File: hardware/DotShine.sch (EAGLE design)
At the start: 55 parts, among them CN1 1X4-BIG, IC1 CAT24M010TS, IC3 SI1145, J3 USB-MICROB, U1 ATMEGA328P-MU-QFN32, U2 TMP102, U3 ATSHA204-TSU, X2 MC-RTC-RV-4162-C7-I2C, X3 S4B-ZR

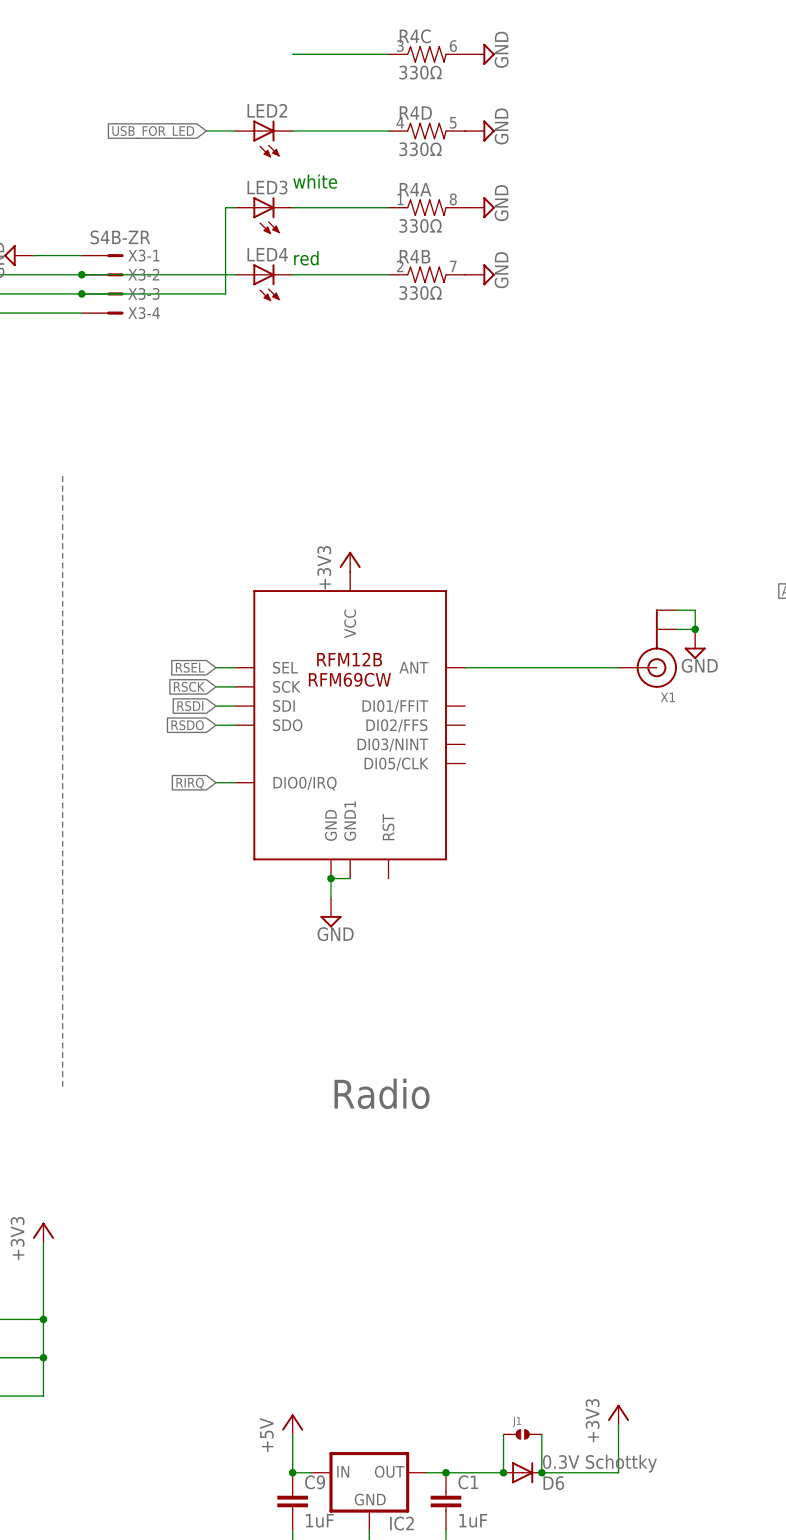
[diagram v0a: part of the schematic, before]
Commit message: Add RST led
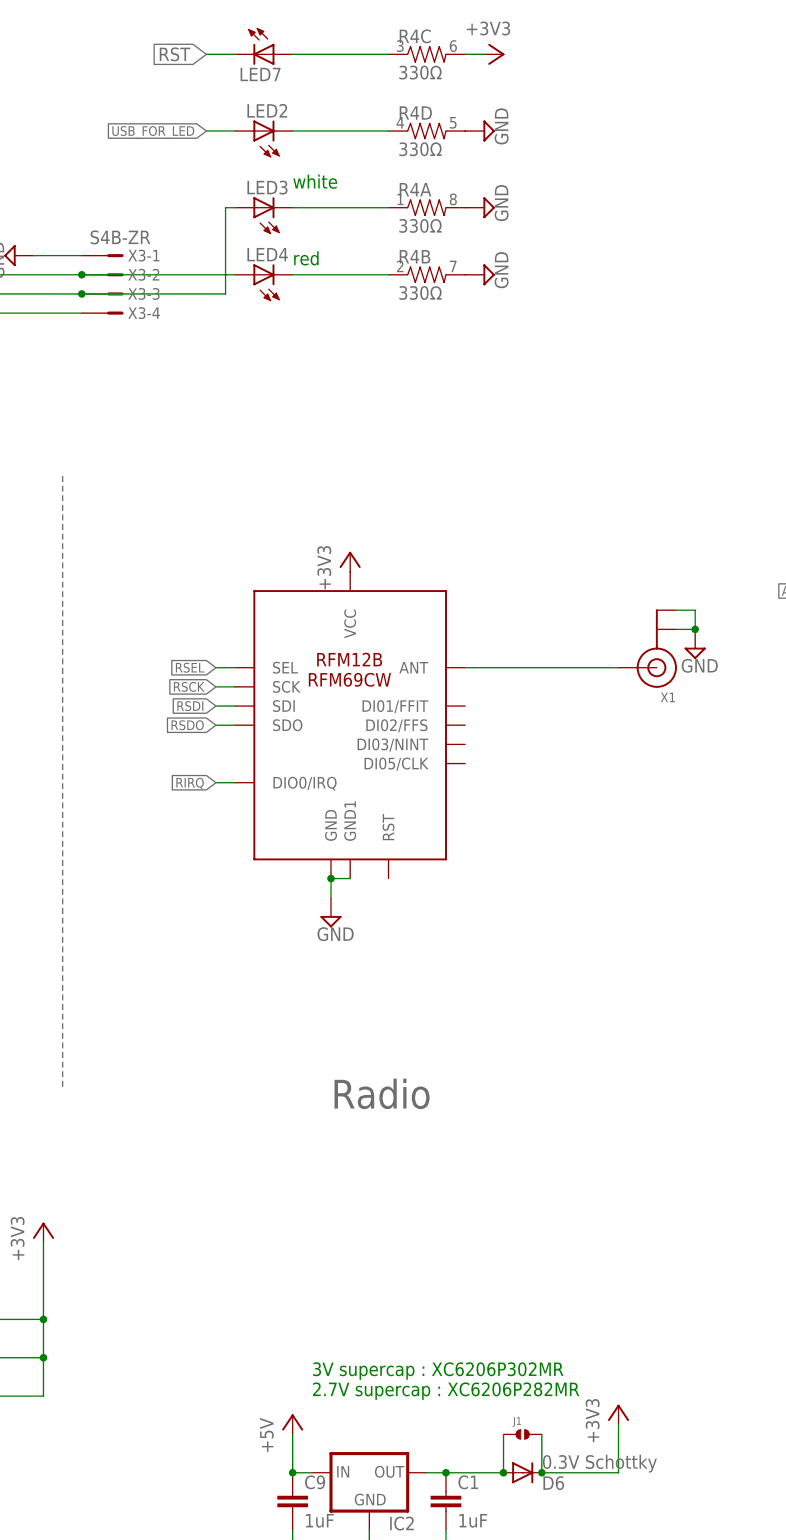
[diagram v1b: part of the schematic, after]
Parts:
- added LED7: (no value), SparkFun:LED0603
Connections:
- net +3V3: now also R4C.2
- net GND: no longer R4C.2
- net N$10: now also LED7.A
- net RST: now also LED7.C
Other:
- note added: "3V supercap : XC6206P302MR 2.7V supercap : XC6206P282MR"
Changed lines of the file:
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@@
 <setting verticaltext="up"/>
 </settings>
-<grid distance="0.1" unitdist="inch" unit="inch" style="lines" multiple="1" display="no" altdistance="0.01" altunitdist="inch" altunit="inch"/>
+<grid distance="0.05" unitdist="inch" unit="inch" style="lines" multiple="1" display="no" altdistance="0.01" altunitdist="inch" altunit="inch"/>
 <layers>
 <layer number="1" name="Top" color="4" fill="1" visible="no" active="no"/>
@@
 <part name="+3V7" library="supply1" deviceset="+3V3" device=""/>
 <part name="R4" library="SparkFun" deviceset="RESISTOR-ARRAY" device="0603-ARV" value="330Ω"/>
-<part name="SUPPLY12" library="supply2" deviceset="GND" device=""/>
 <part name="SUPPLY27" library="supply2" deviceset="GND" device=""/>
 <part name="+3V19" library="supply1" deviceset="+3V3" device=""/>
@@
 <part name="P+5" library="supply1" deviceset="+5V" device=""/>
 <part name="D4" library="diode" deviceset="DIODE-" device="SOD523" value="0.3V Schottky"/>
+<part name="+3V1" library="supply1" deviceset="+3V3" device=""/>
+<part name="LED7" library="SparkFun" deviceset="LED" device="0603"/>
 </parts>
 <sheets>
@@
 <text x="30.48" y="-243.84" size="1.778" layer="91">1000uF .. 6V -&gt; 300uF .. 2V ; 600 .. 3.6V -&gt; buget: 600-300 = 300uF
 1500uF .. 4V -&gt; 750uF .. 2V ; 1350.. 3.6V-&gt; buget: 1350-750 = 600uF</text>
+<text x="137.16" y="-25.4" size="1.778" layer="91">3V supercap : XC6206P302MR
+2.7V supercap : XC6206P282MR</text>
 </plain>
 <instances>
@@
 <instance part="R4" gate="C" x="152.4" y="152.4"/>
 <instance part="R4" gate="D" x="152.4" y="142.24"/>
-<instance part="SUPPLY12" gate="GND" x="160.02" y="152.4" rot="R90"/>
 <instance part="SUPPLY27" gate="GND" x="144.78" y="-48.26" rot="MR0"/>
 <instance part="+3V19" gate="G$1" x="177.8" y="-26.67"/>
@@
 <instance part="P+5" gate="1" x="31.75" y="-205.74"/>
 <instance part="D4" gate="G$1" x="69.85" y="-48.26" rot="MR0"/>
+<instance part="+3V1" gate="G$1" x="162.56" y="152.4" rot="R270"/>
+<instance part="LED7" gate="G$1" x="132.08" y="152.4" rot="R270"/>
 </instances>
 <busses>
@@
 <pinref part="SUPPLY8" gate="GND" pin="GND"/>
 <pinref part="R4" gate="A" pin="2"/>
-</segment>
-<segment>
-<pinref part="R4" gate="C" pin="2"/>
-<pinref part="SUPPLY12" gate="GND" pin="GND"/>
 </segment>
 <segment>
@@
 <wire x1="60.96" y1="118.11" x2="52.07" y2="118.11" width="0.1524" layer="91"/>
 <label x="52.07" y="118.11" size="1.27" layer="95" rot="R180" xref="yes"/>
+</segment>
+<segment>
+<pinref part="LED7" gate="G$1" pin="C"/>
+<wire x1="127" y1="152.4" x2="123.19" y2="152.4" width="0.1524" layer="91"/>
+<label x="123.19" y="152.4" size="1.778" layer="95" rot="R180" xref="yes"/>
 </segment>
 </net>
@@
 <wire x1="167.64" y1="-35.56" x2="177.8" y2="-35.56" width="0.1524" layer="91"/>
 <wire x1="177.8" y1="-35.56" x2="177.8" y2="-29.21" width="0.1524" layer="91"/>
+</segment>
+<segment>
+<pinref part="R4" gate="C" pin="2"/>
+<pinref part="+3V1" gate="G$1" pin="+3V3"/>
+<wire x1="157.48" y1="152.4" x2="160.02" y2="152.4" width="0.1524" layer="91"/>
 </segment>
 </net>
@@
 </segment>
 </net>
-<net name="N$10" class="0">
-<segment>
-<pinref part="R4" gate="C" pin="1"/>
-<wire x1="147.32" y1="152.4" x2="134.62" y2="152.4" width="0.1524" layer="91"/>
-</segment>
-</net>
 <net name="N$11" class="0">
 <segment>
@@
 </segment>
 </net>
+<net name="N$10" class="0">
+<segment>
+<pinref part="LED7" gate="G$1" pin="A"/>
+<pinref part="R4" gate="C" pin="1"/>
+<wire x1="134.62" y1="152.4" x2="147.32" y2="152.4" width="0.1524" layer="91"/>
+</segment>
+</net>

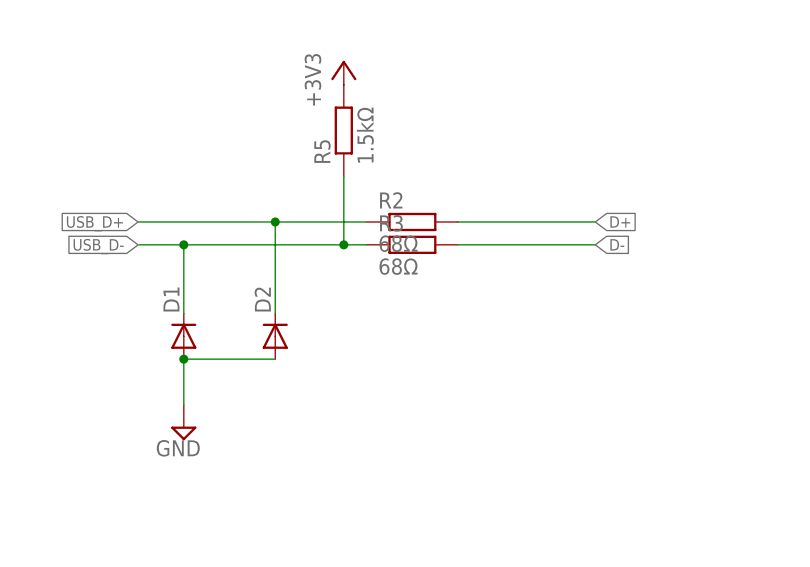
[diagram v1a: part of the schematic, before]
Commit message: Invert cap, improve GND
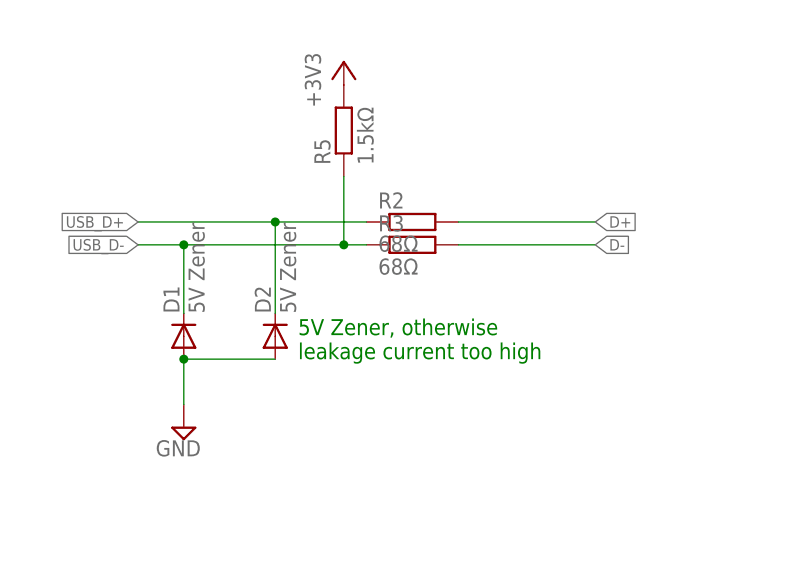
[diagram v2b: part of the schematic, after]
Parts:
- D1, D2: value (none) -> 5V Zener
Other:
- note added: "5V Zener, otherwise leakage current too high"
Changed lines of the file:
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@@
 <setting verticaltext="up"/>
 </settings>
-<grid distance="0.05" unitdist="inch" unit="inch" style="lines" multiple="1" display="no" altdistance="0.01" altunitdist="inch" altunit="inch"/>
+<grid distance="0.1" unitdist="inch" unit="inch" style="lines" multiple="1" display="no" altdistance="0.01" altunitdist="inch" altunit="inch"/>
 <layers>
 <layer number="1" name="Top" color="4" fill="1" visible="no" active="no"/>
@@
 <part name="+3V12" library="supply1" deviceset="+3V3" device=""/>
 <part name="JP2" library="SparkFun-Jumpers" deviceset="JUMPER-SMT_3_1-NC_TRACE" device="_NO-SILK"/>
-<part name="D1" library="diode" deviceset="DIODE-" device="SOD523"/>
-<part name="D2" library="diode" deviceset="DIODE-" device="SOD523"/>
+<part name="D1" library="diode" deviceset="DIODE-" device="SOD523" value="5V Zener"/>
+<part name="D2" library="diode" deviceset="DIODE-" device="SOD523" value="5V Zener"/>
 <part name="SUPPLY14" library="supply2" deviceset="GND" device=""/>
 <part name="R2" library="rcl" deviceset="R-EU_" device="R0603" value="68Ω"/>
@@
 <text x="137.16" y="-25.4" size="1.778" layer="91">3V supercap : XC6206P302MR
 2.7V supercap : XC6206P282MR</text>
+<text x="248.92" y="-71.12" size="1.778" layer="91">5V Zener, otherwise
+leakage current too high </text>
 </plain>
 <instances>

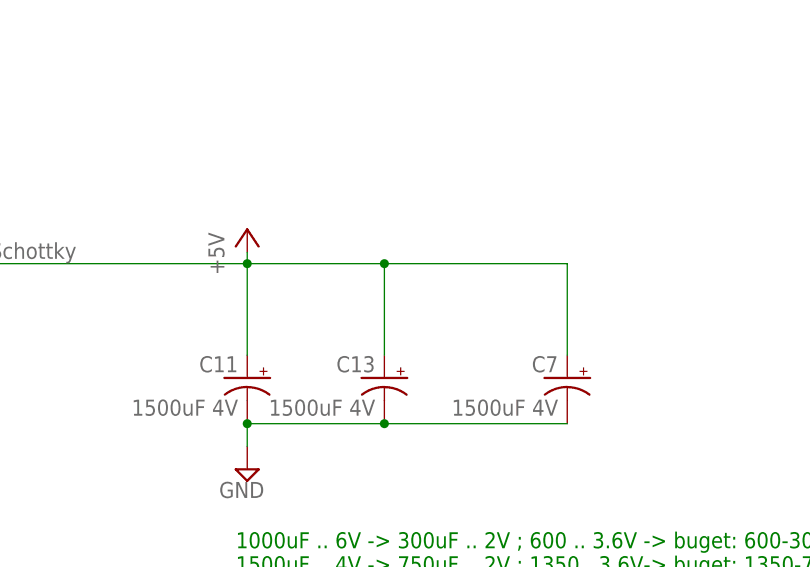
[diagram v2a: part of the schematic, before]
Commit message: Refactor Caps from 5V to 3.3V, update version
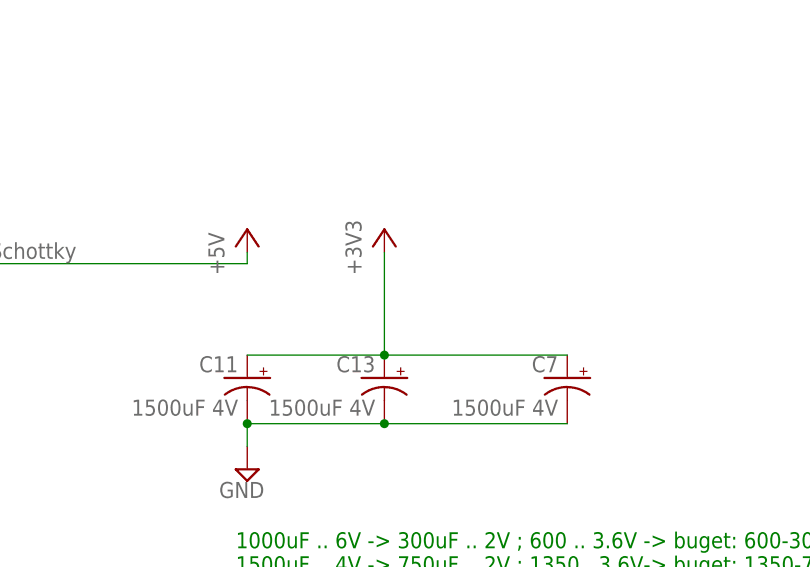
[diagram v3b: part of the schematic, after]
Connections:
- net +3V3: now also C11.+, C13.+, C7.+
- net +5V: no longer C11.+, C13.+, C7.+
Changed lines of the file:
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@@
 <setting verticaltext="up"/>
 </settings>
-<grid distance="0.1" unitdist="inch" unit="inch" style="lines" multiple="1" display="no" altdistance="0.01" altunitdist="inch" altunit="inch"/>
+<grid distance="0.05" unitdist="inch" unit="inch" style="lines" multiple="1" display="no" altdistance="0.01" altunitdist="inch" altunit="inch"/>
 <layers>
 <layer number="1" name="Top" color="4" fill="1" visible="no" active="no"/>
@@
 <part name="+3V1" library="supply1" deviceset="+3V3" device=""/>
 <part name="LED7" library="SparkFun" deviceset="LED" device="0603"/>
+<part name="+3V3" library="supply1" deviceset="+3V3" device=""/>
 </parts>
 <sheets>
@@
 <instance part="+3V1" gate="G$1" x="162.56" y="152.4" rot="R270"/>
 <instance part="LED7" gate="G$1" x="132.08" y="152.4" rot="R270"/>
+<instance part="+3V3" gate="G$1" x="46.99" y="-205.74"/>
 </instances>
 <busses>
@@
 <wire x1="157.48" y1="152.4" x2="160.02" y2="152.4" width="0.1524" layer="91"/>
 </segment>
+<segment>
+<pinref part="C11" gate="G$1" pin="+"/>
+<pinref part="C13" gate="G$1" pin="+"/>
+<wire x1="31.75" y1="-219.71" x2="46.99" y2="-219.71" width="0.1524" layer="91"/>
+<pinref part="C7" gate="G$1" pin="+"/>
+<wire x1="46.99" y1="-219.71" x2="67.31" y2="-219.71" width="0.1524" layer="91"/>
+<junction x="46.99" y="-219.71"/>
+<pinref part="+3V3" gate="G$1" pin="+3V3"/>
+<wire x1="46.99" y1="-208.28" x2="46.99" y2="-219.71" width="0.1524" layer="91"/>
+</segment>
 </net>
 <net name="ADCENA" class="0">
@@
 <wire x1="-2.54" y1="-209.55" x2="31.75" y2="-209.55" width="0.1524" layer="91"/>
 <wire x1="31.75" y1="-209.55" x2="31.75" y2="-208.28" width="0.1524" layer="91"/>
-<pinref part="C11" gate="G$1" pin="+"/>
-<wire x1="31.75" y1="-209.55" x2="31.75" y2="-219.71" width="0.1524" layer="91"/>
-<junction x="31.75" y="-209.55"/>
-<pinref part="C13" gate="G$1" pin="+"/>
-<wire x1="46.99" y1="-219.71" x2="46.99" y2="-209.55" width="0.1524" layer="91"/>
-<wire x1="46.99" y1="-209.55" x2="31.75" y2="-209.55" width="0.1524" layer="91"/>
-<pinref part="C7" gate="G$1" pin="+"/>
-<wire x1="67.31" y1="-219.71" x2="67.31" y2="-209.55" width="0.1524" layer="91"/>
-<wire x1="67.31" y1="-209.55" x2="46.99" y2="-209.55" width="0.1524" layer="91"/>
-<junction x="46.99" y="-209.55"/>
-</segment>
-<segment>
+</segment>
+<segment>
